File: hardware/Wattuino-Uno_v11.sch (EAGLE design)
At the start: 18 parts, among them IC2 ATTINY85-MU, J1 USB-MICRO, J2 MA04-1, J3 MA04-1, SW1 SW-TACTILE-PTS840P, X1 PASSER-07, X2 PASSER-07, X3 PASSER-07

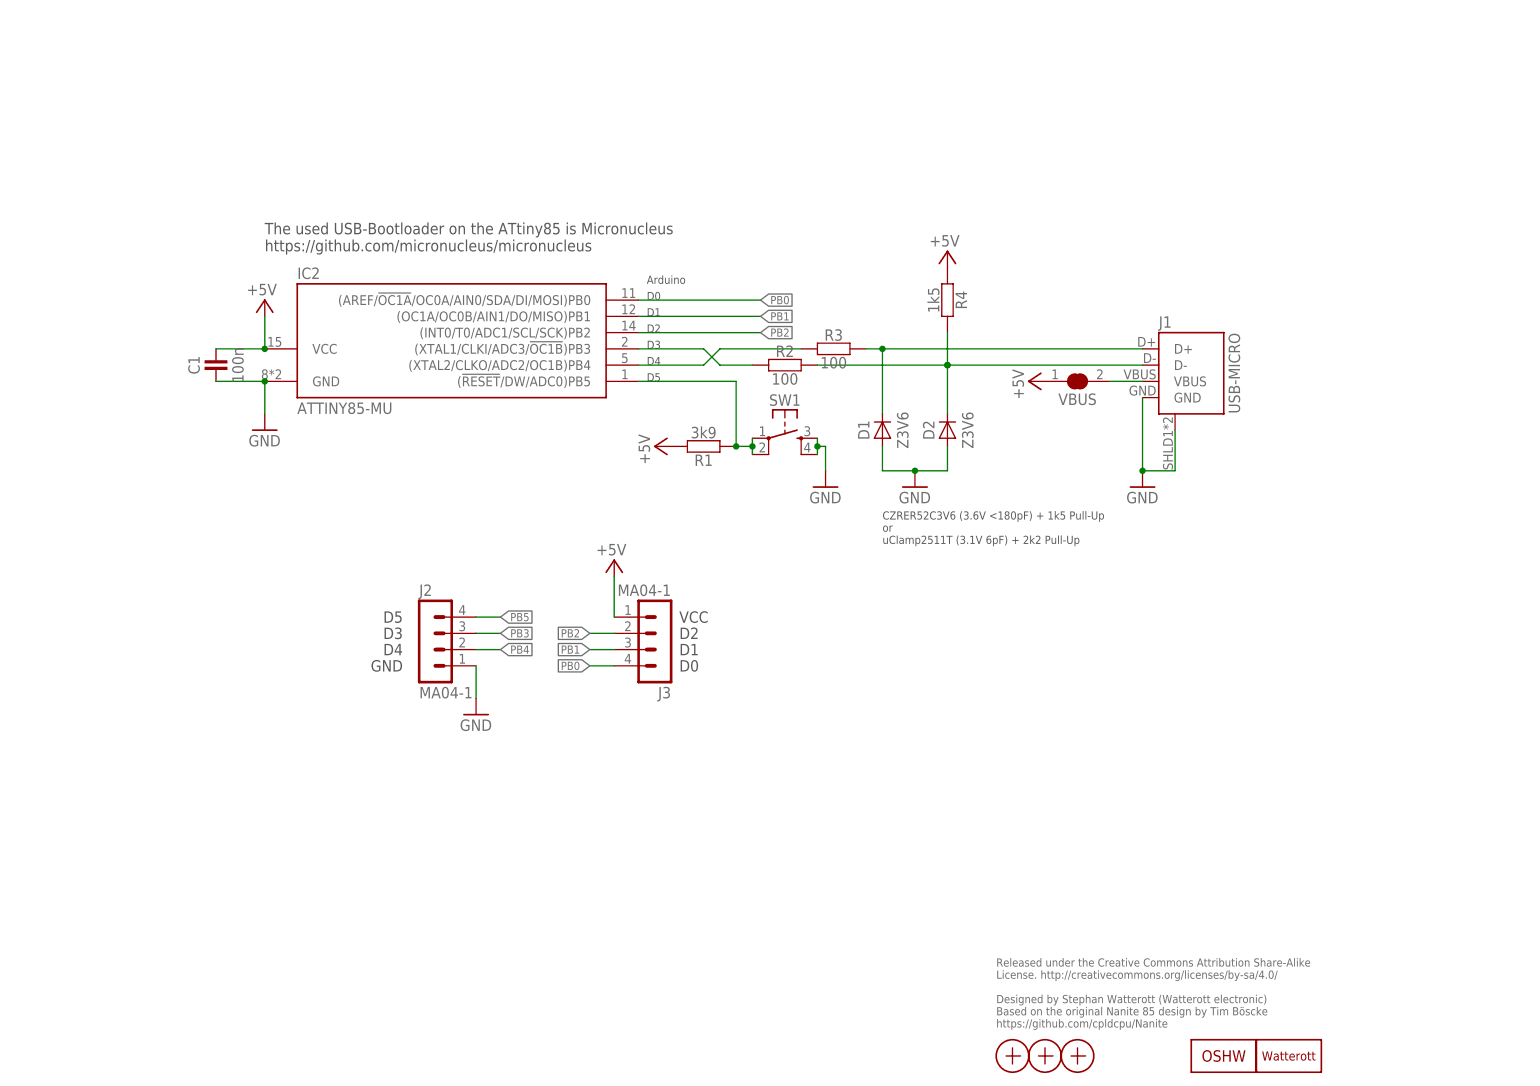
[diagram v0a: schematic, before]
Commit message: updated schematics
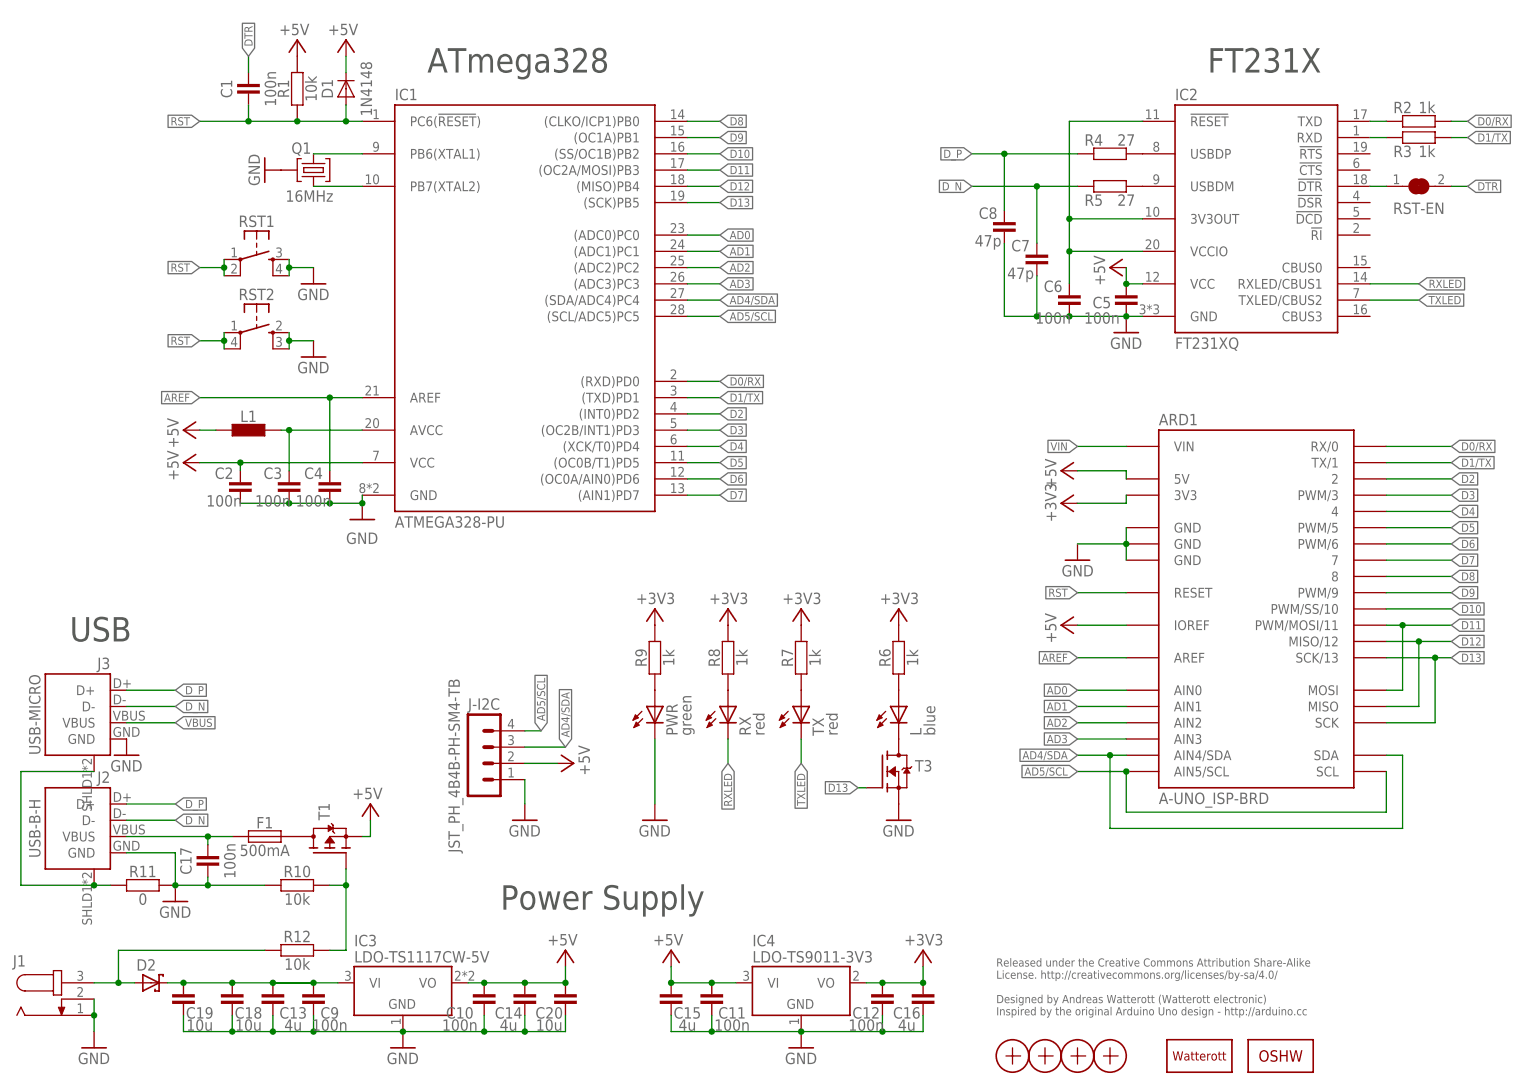
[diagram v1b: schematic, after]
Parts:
- removed SW1: SW-TACTILE-PTS840P, we-switch:SW-TACTILE-PTS840P
- removed VBUS: JUMPER2-0603-NC, we-rcl:JUMPER2-0603-NC
- added ARD1: A-UNO_ISP-BRD, we-board:A-UNO_ISP-BRD
- added C10, C11, C12, C17, C2, C3, C4, C5, C6, C9: 100n, we-rcl:CAPACITOR-0402
- added C13, C14, C15, C16: 4u, we-rcl:CAPACITOR-0603
- added C18, C19, C20: 10u, we-rcl:CAPACITOR-1206
- added C7, C8: 47p, we-rcl:CAPACITOR-0402
- added F1: 500mA, we-rcl:FUSE-0805
- added IC1: ATMEGA328-PU, we-chip:ATMEGA328-PU
- added IC3: LDO-TS1117CW-5V, we-power:LDO-TS1117CW-5V
- added IC4: LDO-TS9011-3V3, we-power:LDO-TS9011-3V3
- added J-I2C: JST_PH_4B4B-PH-SM4-TB, we-con:JST_PH_4B4B-PH-SM4-TB
- added L: blue, we-opto:LED-0603
- added L1: (no value), we-rcl:INDUCTOR-0603
- added PWR: green, we-opto:LED-0603
- added Q1: 16MHz, we-rcl:CRYSTAL-RES-32
- added R10, R12: 10k, we-rcl:RESISTOR-0402
- added R11: 0, we-rcl:RESISTOR-0402
- added R5: 27, we-rcl:RESISTOR-0402
- added R6, R7, R8, R9: 1k, we-rcl:RESISTOR-0402
- added RST-EN: JUMPER2-0603, we-rcl:JUMPER2-0603
- added RST1: SW-TACTILE-PTS840P, we-switch:SW-TACTILE-PTS840P
- added RST2: SW-TACTILE-TL3315, we-switch:SW-TACTILE-TL3315
- added RX, TX: red, we-opto:LED-0603
- added T1: (no value), we-transistor:MOSFET-P-SOT23
- added T3: (no value), we-transistor:MOSFET-N-SOT23
- added X4: PASSER-07, we-symbol:PASSER-07
- D1: value Z3V6 -> 1N4148; device we-rcl:DIODE-SOD882 -> we-rcl:DIODE-SOD110
- D2: value Z3V6 -> (none); device we-rcl:DIODE-SOD882 -> we-rcl:D_SCHOTTKY-SMA
- IC2: value ATTINY85-MU -> FT231XQ; device we-chip:ATTINY85-MU -> we-chip:FT231XQ
- J1: value USB-MICRO -> (none); device we-con:USB-MICRO -> we-con:DC-JACK
- J2: value MA04-1 -> USB-B-H; device we-con:MA04-1 -> we-con:USB-B-H
- J3: value MA04-1 -> USB-MICRO; device we-con:MA04-1 -> we-con:USB-MICRO
- LOGO1: value LOGO-S_PLACE_S -> LOGO-S_PLACE_M; device we-symbol:LOGO-S_PLACE_S -> we-symbol:LOGO-S_PLACE_M
- LOGO2: value OSHW_LOGOX0070 -> OSHW_LOGOX0100; device we-symbol:OSHW_LOGOX0070 -> we-symbol:OSHW_LOGOX0100
- R1: value 3k9 -> 10k
- R2, R3: value 100 -> 1k
- R4: value 1k5 -> 27
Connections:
- removed net PB0: IC2.(AREF/!OC1A!/OC0A/AIN0/SDA/DI/MOSI)PB0, J3.4
- removed net PB1: IC2.(OC1A/OC0B/AIN1/DO/MISO)PB1, J3.3
- removed net PB2: IC2.(INT0/T0/ADC1/SCL/SCK)PB2, J3.2
- removed net PB3: IC2.(XTAL1/CLKI/ADC3/!OC1B!)PB3, J2.3, R2.1
- removed net PB4: IC2.(XTAL2/CLKO/ADC2/OC1B)PB4, J2.2, R3.1
- removed net PB5: IC2.(!RESET!/DW/ADC0)PB5, J2.4, R1.1, SW1.P1, SW1.P2
- new net +3V3: ARD1.3V3, C12.2, C16.2, IC4.VO, R6.2, R7.2, R8.2, R9.2
- new net 3V3OUT: C6.2, IC2.!RESET, IC2.3V3OUT, IC2.VCCIO
- new net AD0: ARD1.AIN0, IC1.(ADC0)PC0
- new net AD1: ARD1.AIN1, IC1.(ADC1)PC1
- new net AD2: ARD1.AIN2, IC1.(ADC2)PC2
- new net AD3: ARD1.AIN3, IC1.(ADC3)PC3
- new net AD4/SDA: ARD1.AIN4/SDA, ARD1.SDA, IC1.(SDA/ADC4)PC4, J-I2C.3
- new net AD5/SCL: ARD1.AIN5/SCL, ARD1.SCL, IC1.(SCL/ADC5)PC5, J-I2C.4
- new net AREF: ARD1.AREF, C4.2, IC1.AREF
- new net AVCC: C3.2, IC1.AVCC, L1.2
- new net D0/RX: ARD1.RX/0, IC1.(RXD)PD0, R2.2
- new net D1/TX: ARD1.TX/1, IC1.(TXD)PD1, R3.2
- new net D10: ARD1.PWM/SS/10, IC1.(SS/OC1B)PB2
- new net D11: ARD1.MOSI, ARD1.PWM/MOSI/11, IC1.(OC2A/MOSI)PB3
- new net D12: ARD1.MISO, ARD1.MISO/12, IC1.(MISO)PB4
- new net D13: ARD1.SCK, ARD1.SCK/13, IC1.(SCK)PB5, T3.G
- new net D2: ARD1.2, IC1.(INT0)PD2
- new net D3: ARD1.PWM/3, IC1.(OC2B/INT1)PD3
- new net D4: ARD1.4, IC1.(XCK/T0)PD4
- new net D5: ARD1.PWM/5, IC1.(OC0B/T1)PD5
- new net D6: ARD1.PWM/6, IC1.(OC0A/AIN0)PD6
- new net D7: ARD1.7, IC1.(AIN1)PD7
- new net D8: ARD1.8, IC1.(CLKO/ICP1)PB0
- new net D9: ARD1.PWM/9, IC1.(OC1A)PB1
- new net DN: IC2.USBDM, R5.2
- new net DP: IC2.USBDP, R4.2
- new net DTR: C1.2, RST-EN.2
- new net DTR_FT: IC2.!DTR, RST-EN.1
- new net N$1: PWR.A, R9.1
- new net N$10: R8.1, RX.A
- new net N$7: L.C, T3.D
- new net N$8: L.A, R6.1
- new net N$9: R7.1, TX.A
- new net RST: ARD1.RESET, C1.1, D1.A, IC1.PC6(!RESET!), R1.1, RST1.P1, RST1.P2, RST2.P1, RST2.P2
- new net RXLED: IC2.RXLED/CBUS1, RX.C
- new net RX_FT: IC2.RXD, R3.1
- new net SHLD: J2.SHIELD, J3.SHIELD, R11.1
- new net TXLED: IC2.TXLED/CBUS2, TX.C
- new net TX_FT: IC2.TXD, R2.1
- new net USBVCC: F1.2, T1.D
- new net VEXT: D2.A, J1.3, R12.1
- new net VEXT2: R10.2, R12.2, T1.G
- new net VIN: ARD1.VIN, C13.2, C18.2, C19.2, C9.2, D2.C, IC3.VI
- new net XTAL1: IC1.PB6(XTAL1), Q1.2
- new net XTAL2: IC1.PB7(XTAL2), Q1.1
- net +5V: now also ARD1.5V, ARD1.IOREF, C10.2, C11.2, C14.2, C15.2, C2.2, C20.2, C5.2, D1.C, IC1.VCC, IC3.VO, IC4.VI, J-I2C.2, L1.1, T1.S; no longer C1.2, J3.1, R4.1, VBUS.1
- net D_N: now also C7.2, J2.D-, J3.D-, R5.1; no longer D2.C, J1.D-, R2.2, R4.2
- net D_P: now also C8.2, J2.D+, J3.D+, R4.1; no longer D1.C, J1.D+, R3.2
- net GND: now also ARD1.GND@1, ARD1.GND@2, ARD1.GND@3, C10.1, C11.1, C12.1, C13.1, C14.1, C15.1, C16.1, C17.1, C18.1, C19.1, C2.1, C20.1, C3.1, C4.1, C5.1, C6.1, C7.1, C8.1, C9.1, IC1.GND, IC3.GND, IC4.GND, J-I2C.1, J1.1, J1.2, J2.GND, J3.GND, PWR.C, Q1.GND, R10.1, R11.2, RST1.S1, RST1.S2, RST2.S1, RST2.S2, T3.S; no longer C1.1, D1.A, D2.A, J1.GND, J1.SHIELD, J2.1, SW1.S1, SW1.S2
- net VBUS: now also C17.2, F1.1, J2.VBUS, J3.VBUS; no longer J1.VBUS, VBUS.2
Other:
- note added: "ATmega328"
- note added: "FT231X"
- note added: "Power Supply"
- note added: "Released under the Creative Commons Attribution Share-Alike License. http://creativecommons.org/licenses/by-sa/4.0/ Designed by Andreas Watterott (Watterott electronic) Inspired by the original Arduino Uno design - http://arduino.cc"
- note added: "USB"
- note removed: "ATtiny85 AVR"
- note removed: "Arduino"
- note removed: "CZRER52C3V6 (3.6V <180pF) + 1k5 Pull-Up or uClamp2511T (3.1V 6pF) + 2k2 Pull-Up"
- note removed: "D0"
- note removed: "D1"
- note removed: "D2"
- note removed: "D3"
- note removed: "D4"
- note removed: "D5"
- note removed: "GND"
- note removed: "Released under the Creative Commons Attribution Share-Alike License. http://creativecommons.org/licenses/by-sa/4.0/ Designed by Stephan Watterott (Watterott electronic) Based on the original Nanite 85 design by Tim Böscke https://github.com/cpldcpu/Nanite"
- note removed: "The used USB-Bootloader on the ATtiny85 is Micronucleus https://github.com/micronucleus/micronucleus"
- note removed: "VCC"
- moved on the sheet: C1, D1, R1, R2, R3, R4

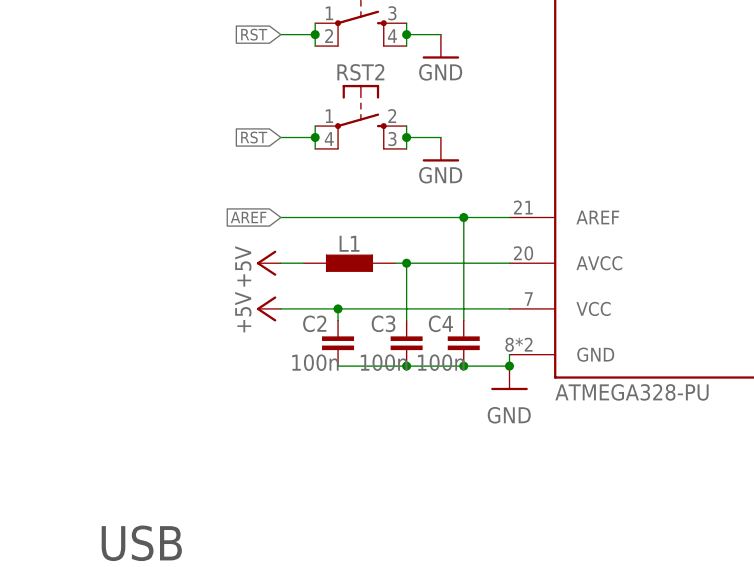
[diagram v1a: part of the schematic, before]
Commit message: updated schematics
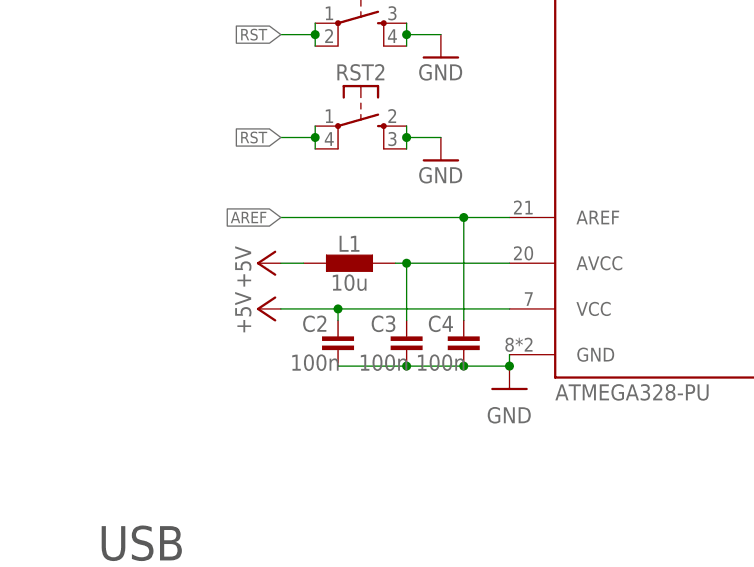
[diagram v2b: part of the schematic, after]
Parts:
- L1: value (none) -> 10u
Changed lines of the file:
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@@
 <setting verticaltext="up"/>
 </settings>
-<grid distance="0.05" unitdist="inch" unit="inch" style="lines" multiple="1" display="yes" altdistance="0.025" altunitdist="inch" altunit="inch"/>
+<grid distance="0.1" unitdist="inch" unit="inch" style="lines" multiple="1" display="no" altdistance="0.01" altunitdist="inch" altunit="inch"/>
 <layers>
 <layer number="1" name="Top" color="4" fill="1" visible="no" active="no"/>
@@
 <part name="C17" library="we-rcl" deviceset="CAPACITOR" device="-0402" value="100n"/>
 <part name="C18" library="we-rcl" deviceset="CAPACITOR" device="-1206" value="10u"/>
-<part name="L1" library="we-rcl" deviceset="INDUCTOR" device="-0603"/>
+<part name="L1" library="we-rcl" deviceset="INDUCTOR" device="-0603" value="10u"/>
 <part name="P+10" library="supply1" deviceset="+5V" device=""/>
 <part name="+3V5" library="supply1" deviceset="+3V3" device=""/>
